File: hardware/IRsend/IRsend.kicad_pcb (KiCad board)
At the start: 2 copper layers, 35 x 65 mm, 9 parts, among them J1 Conn_01x03_Pin, U1 WEMOS_D1_mini_V4

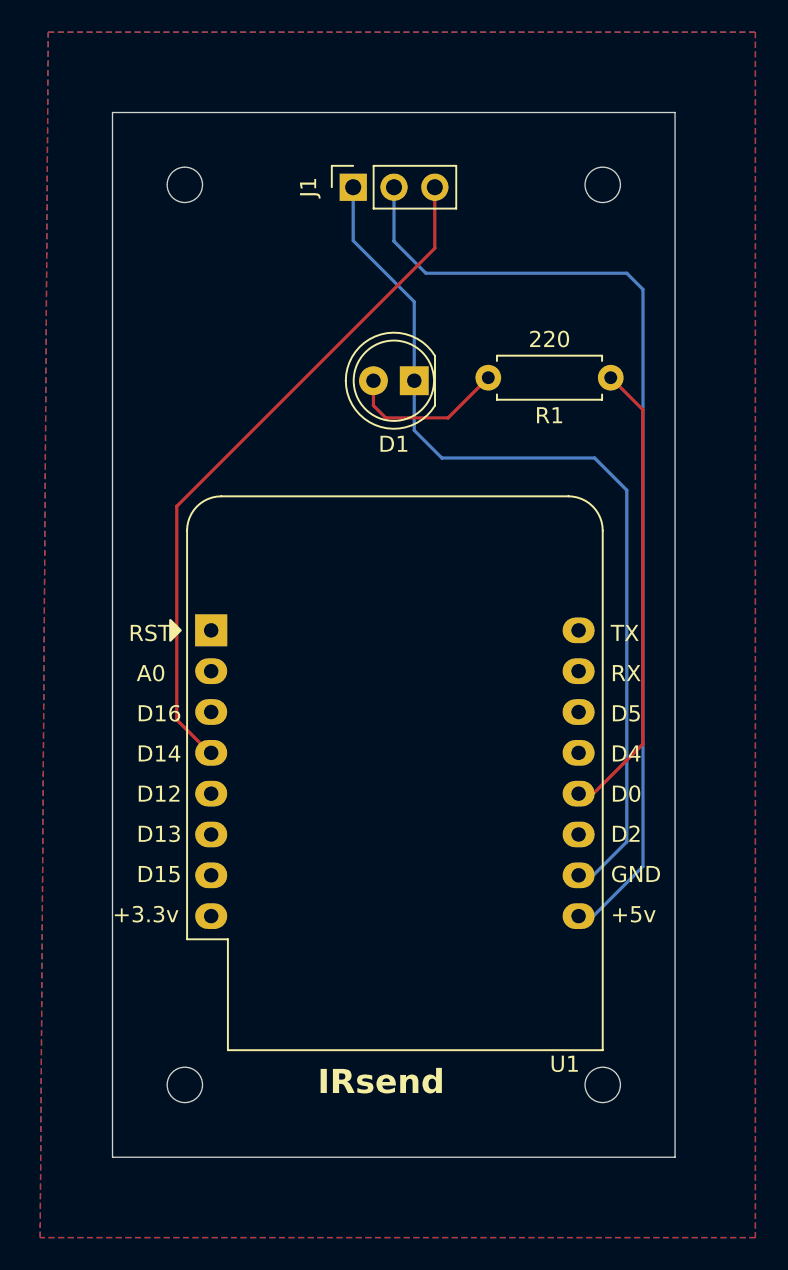
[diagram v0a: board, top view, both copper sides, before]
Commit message: Fixed problem with IR signal and GND being swapped on J1.
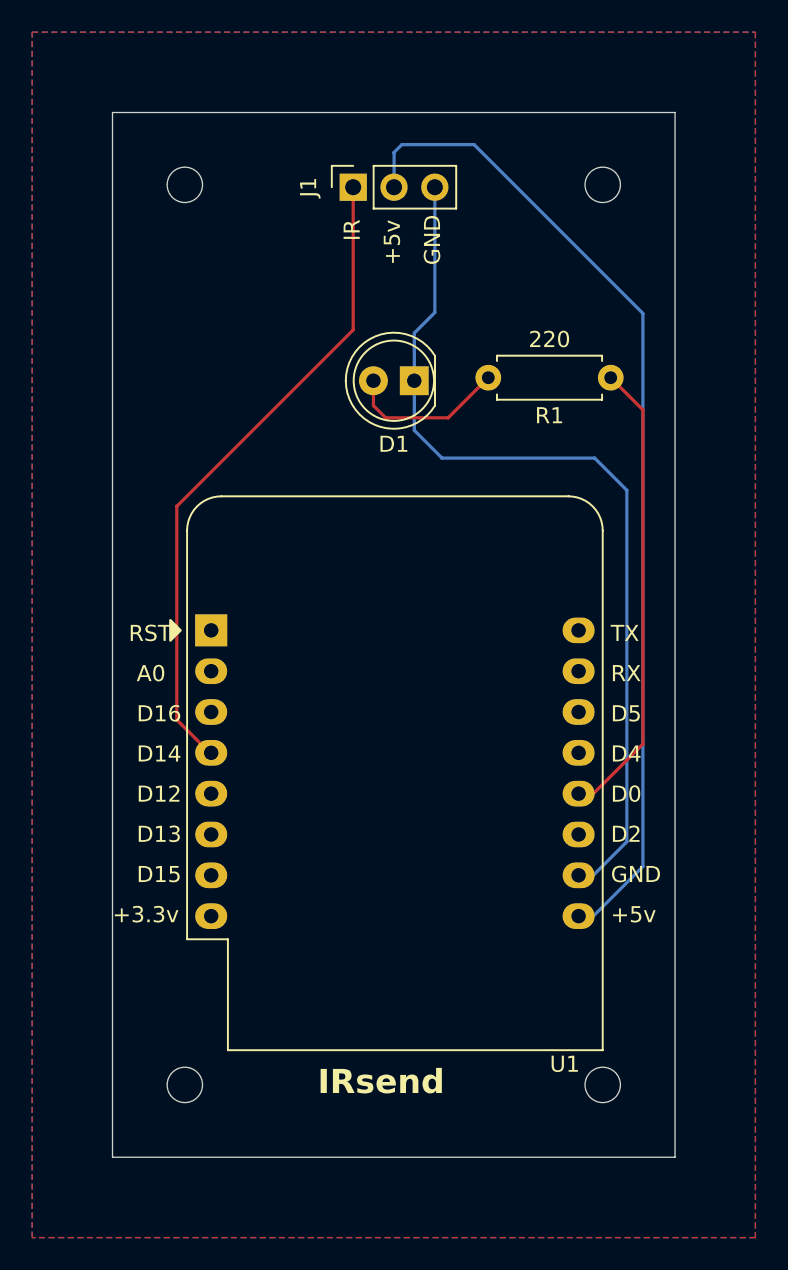
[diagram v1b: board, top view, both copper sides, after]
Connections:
- J1 pad 1: GND -> Net-(J1-Pin_1)
- J1 pad 3: Net-(J1-Pin_3) -> GND
- U1 pad 4: Net-(J1-Pin_3) -> Net-(J1-Pin_1)
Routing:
- net Net-(J1-Pin_3): track 43.4 -> 0.00 mm
- net Net-(J1-Pin_1): track 0.00 -> 41.3 mm
- net GND: track 57.0 -> 56.0 mm
- net Net-(J1-Pin_2): track 61.1 -> 61.7 mm
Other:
- board text added: "IR"
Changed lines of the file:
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@@
 	(net 1 "GND")
 	(net 2 "Net-(D1-A)")
-	(net 3 "Net-(J1-Pin_3)")
+	(net 3 "Net-(J1-Pin_1)")
 	(net 4 "Net-(J1-Pin_2)")
 	(net 5 "Net-(U1-D0)")
@@
 			(layers "*.Cu" "*.Mask")
 			(remove_unused_layers no)
-			(net 3 "Net-(J1-Pin_3)")
+			(net 3 "Net-(J1-Pin_1)")
 			(pinfunction "SCK/D14")
 			(pintype "bidirectional")
@@
 			(layers "*.Cu" "*.Mask")
 			(remove_unused_layers no)
-			(net 1 "GND")
+			(net 3 "Net-(J1-Pin_1)")
 			(pinfunction "Pin_1")
 			(pintype "passive")
@@
 			(layers "*.Cu" "*.Mask")
 			(remove_unused_layers no)
-			(net 3 "Net-(J1-Pin_3)")
+			(net 1 "GND")
 			(pinfunction "Pin_3")
 			(pintype "passive")
@@
 		)
 	)
+	(gr_text "IR"
+		(at 165.5 78 90)
+		(layer "F.SilkS")
+		(effects
+			(font
+				(size 1 1)
+				(thickness 0.1)
+			)
+			(justify left bottom)
+		)
+	)
 	(gr_text "+3.3v"
 		(at 150 120.5 0)
@@
 		)
 	)
+	(gr_text "GND"
+		(at 170.5 79.5 90)
+		(layer "F.SilkS")
+		(effects
+			(font
+				(size 1 1)
+				(thickness 0.1)
+			)
+			(justify left bottom)
+		)
+	)
 	(gr_text "D16"
 		(at 151.5 108 0)
@@
 	(gr_text "A0"
 		(at 151.5 105.5 0)
+		(layer "F.SilkS")
+		(effects
+			(font
+				(size 1 1)
+				(thickness 0.1)
+			)
+			(justify left bottom)
+		)
+	)
+	(gr_text "+5v"
+		(at 168 79.5 90)
 		(layer "F.SilkS")
 		(effects
@@
 	)
 	(segment
-		(start 168.775 86.688024)
-		(end 168.775 81.775)
+		(start 170.5 91.5)
+		(end 168.775 89.775)
 		(width 0.2)
 		(layer "B.Cu")
@@
 	)
 	(segment
-		(start 168.775 81.775)
-		(end 164.975 77.975)
+		(start 170.055 82.445)
+		(end 170.055 74.648024)
 		(width 0.2)
 		(layer "B.Cu")
@@
 	)
 	(segment
-		(start 170.5 91.5)
-		(end 168.775 89.775)
+		(start 182 93.5)
+		(end 180 91.5)
 		(width 0.2)
 		(layer "B.Cu")
@@
 	)
 	(segment
-		(start 182 93.5)
-		(end 180 91.5)
+		(start 179.415 117.96)
+		(end 182 115.375)
 		(width 0.2)
 		(layer "B.Cu")
@@
 	)
 	(segment
-		(start 179.415 117.96)
-		(end 182 115.375)
+		(start 180 91.5)
+		(end 170.5 91.5)
 		(width 0.2)
 		(layer "B.Cu")
@@
 	)
 	(segment
-		(start 180 91.5)
-		(end 170.5 91.5)
+		(start 168.775 89.775)
+		(end 168.775 86.688024)
 		(width 0.2)
 		(layer "B.Cu")
@@
 	)
 	(segment
-		(start 164.975 77.975)
-		(end 164.975 74.648024)
+		(start 182 115.375)
+		(end 182 93.5)
 		(width 0.2)
 		(layer "B.Cu")
@@
 	)
 	(segment
-		(start 168.775 89.775)
-		(end 168.775 86.688024)
+		(start 168.775 83.725)
+		(end 170.055 82.445)
 		(width 0.2)
 		(layer "B.Cu")
@@
 	)
 	(segment
-		(start 182 115.375)
-		(end 182 93.5)
+		(start 168.775 86.688024)
+		(end 168.775 83.725)
 		(width 0.2)
 		(layer "B.Cu")
@@
 	)
 	(segment
-		(start 170.055 78.445)
-		(end 154 94.5)
+		(start 164.975 83.525)
+		(end 164.975 74.648024)
 		(width 0.2)
 		(layer "F.Cu")
@@
 	)
 	(segment
-		(start 170.055 74.648024)
-		(end 170.055 78.445)
+		(start 154 94.5)
+		(end 154 107.785)
 		(width 0.2)
 		(layer "F.Cu")
@@
 	(segment
 		(start 154 94.5)
-		(end 154 107.785)
+		(end 164.975 83.525)
 		(width 0.2)
 		(layer "F.Cu")
@@
 	)
 	(segment
-		(start 183 81)
-		(end 182 80)
+		(start 172.5 72)
+		(end 168 72)
 		(width 0.2)
 		(layer "B.Cu")
@@
 	)
 	(segment
-		(start 183 116.915)
-		(end 183 81)
+		(start 179.415 120.5)
+		(end 183 116.915)
 		(width 0.2)
 		(layer "B.Cu")
@@
 	)
 	(segment
-		(start 167.515 77.985)
-		(end 167.515 74.648024)
+		(start 168 72)
+		(end 167.5 72.5)
 		(width 0.2)
 		(layer "B.Cu")
@@
 	)
 	(segment
-		(start 179.415 120.5)
-		(end 183 116.915)
+		(start 167.515 72.515)
+		(end 167.515 74.648024)
 		(width 0.2)
 		(layer "B.Cu")
@@
 	)
 	(segment
-		(start 167.5 78)
-		(end 167.515 77.985)
+		(start 183 82.5)
+		(end 172.5 72)
 		(width 0.2)
 		(layer "B.Cu")
@@
 	)
 	(segment
-		(start 182 80)
-		(end 169.5 80)
+		(start 183 116.915)
+		(end 183 82.5)
 		(width 0.2)
 		(layer "B.Cu")
@@
 	)
 	(segment
-		(start 169.5 80)
-		(end 167.5 78)
+		(start 167.5 72.5)
+		(end 167.515 72.515)
 		(width 0.2)
 		(layer "B.Cu")
@@
 		(polygon
 			(pts
-				(xy 190 65) (xy 190 140) (xy 145.5 140) (xy 146 65)
-			)
-		)
+				(xy 145 65) (xy 190 65) (xy 190 140) (xy 145 140)
+			)
+		)
